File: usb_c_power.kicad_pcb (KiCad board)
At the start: 2 copper layers, 36 x 12 mm, 27 parts, among them J1 USB4085-GF-A, J2 ‎282837-2‎, Q1 IRF9358TRPBF, U1 CYPD3177

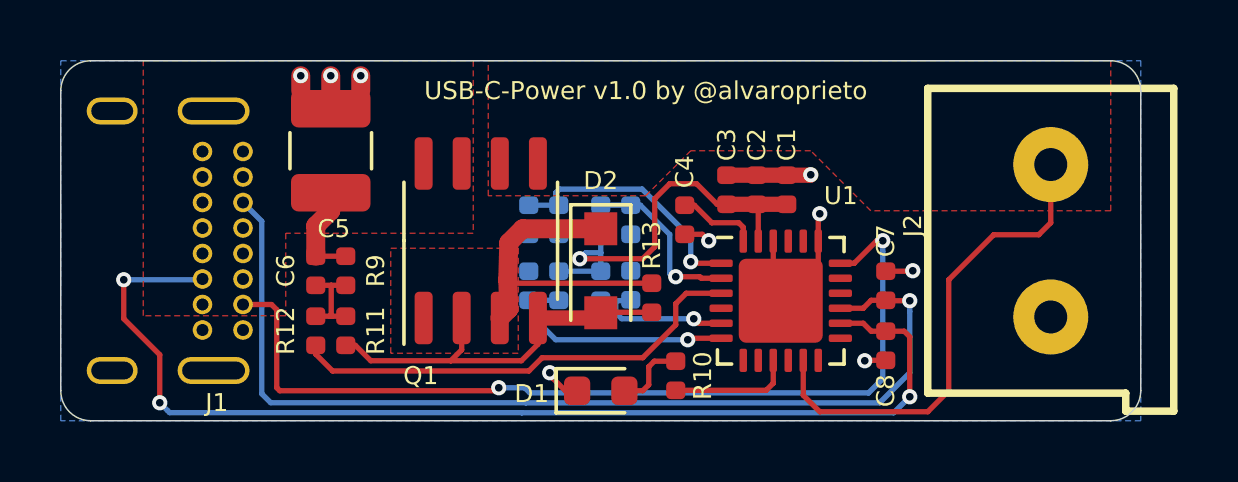
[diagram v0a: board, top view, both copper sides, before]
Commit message: Created v1.1 * much larger (0805) setting resistors * 5A rated USB-C connector * Smaller 10V zener * Paste-in-hole for usb-c
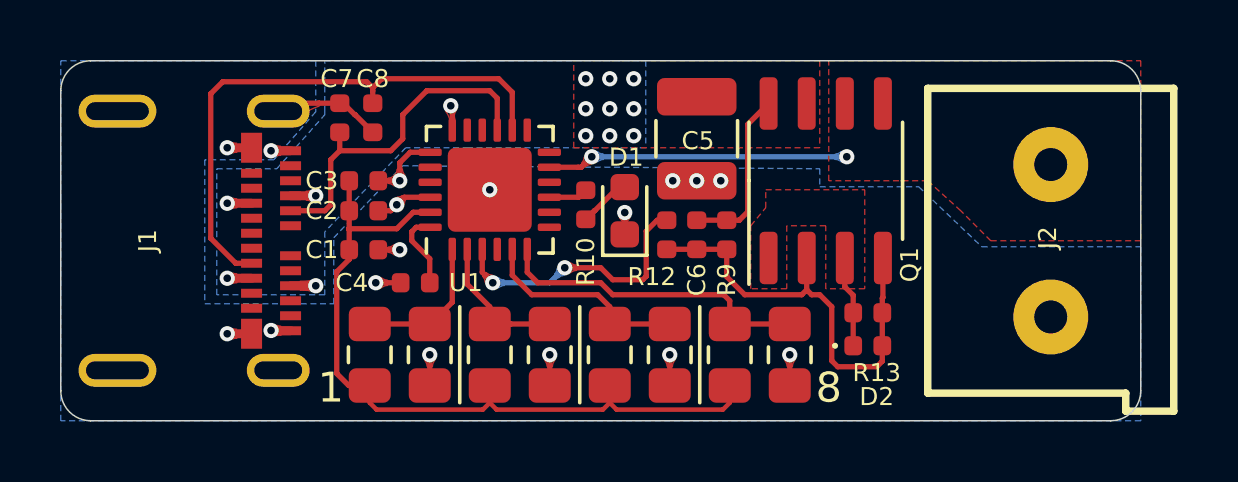
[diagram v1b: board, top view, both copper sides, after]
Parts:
- removed R11: 0, Resistor_SMD:R_0402_1005Metric
- D2: footprint Diode_SMD:D_SOD-123F -> Diode_SMD:D_0402_1005Metric
- J1: value USB4085-GF-A -> USB_C_Receptacle; footprint alvarop:USB4085-GF-A -> alvarop:MOLEX-1054500101
- R1, R2, R3, R4, R5, R6, R7, R8: footprint Resistor_SMD:R_0402_1005Metric -> Resistor_SMD:R_0805_2012Metric_Pad1.15x1.40mm_HandSolder; moved to F.Cu
- moved C7 19.0 mm to (104.3, 95.9)
- moved C8 18.7 mm to (105.4, 95.9)
- moved C1 14.2 mm to (105.1, 100.3), turned to 0 degrees
- moved C2 13.1 mm to (105.1, 99.0), turned to 0 degrees
- moved C6 12.8 mm to (116.2, 99.8)
- moved R9 12.8 mm to (117.2, 99.8)
- moved C5 12.2 mm to (116.2, 96.6), turned to 270 degrees
- moved R12 12.1 mm to (115.2, 99.8), turned to 90 degrees
- moved C3 12.1 mm to (105.1, 98.0), turned to 0 degrees
- moved Q1 11.7 mm to (120.5, 98.0)
- moved U1 10.4 mm to (109.3, 98.3), turned to 90 degrees
- moved D2 9.24 mm to (121.9, 103.5), turned to 0 degrees
- moved C4 9.23 mm to (106.8, 101.4), turned to 180 degrees
- moved R8 9.00 mm to (119.3, 103.8), turned to 270 degrees
- moved R1 7.74 mm to (105.3, 103.8)
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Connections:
- C6 pad 2: Net-(C6-Pad2) -> /FET_GATE
- R12 pad 1: Net-(C6-Pad2) -> /FET_GATE
- R9 pad 2: Net-(C6-Pad2) -> /FET_GATE
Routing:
- net /VBUS_IN: track 34.0 -> 9.85 mm, vias 2 -> 14
- net /CC1: track 33.6 -> 11.7 mm, vias 1 -> 0
- net /CC2: track 37.2 -> 18.9 mm, vias 3 -> 0
- net +3V3: track 15.4 -> 25.7 mm, vias 1 -> 0
- net /FET_SRC: track 10.7 -> 3.04 mm
- net /VBUS_FET_EN: track 15.5 -> 9.13 mm, vias 0 -> 2
- net /DC_OUT: track 16.4 -> 10.1 mm, vias 0 -> 2
- net GND: track 13.5 -> 17.6 mm, vias 9 -> 17
- net /VBUS_MIN: track 8.47 -> 4.81 mm, vias 1 -> 0
- net Net-(C6-Pad2): track 3.02 -> 0.00 mm
- net Net-(R10-Pad1): track 4.11 -> 1.31 mm
- net /ISNK_FINE: track 8.11 -> 10.7 mm, vias 1 -> 0
- net /FET_GATE: track 13.2 -> 15.2 mm
- net /ISNK_COARSE: track 5.06 -> 7.12 mm, vias 1 -> 0
- net /VBUS_MAX: track 5.79 -> 4.80 mm, vias 1 -> 0
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- added copper zone on B.Cu, net /VBUS_IN
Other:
- board text added: "1"
- board text added: "8"
- board text added: "Icoarse"
- board text added: "Ifine"
- board text removed: "Icrs"
- board text removed: "Ifin"

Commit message: Finished v1.1 and ordered from oshpark
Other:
- board text added: "USB-C-Power v1.1 by @alvaroprieto"
- board text removed: "USB-C-Power v1.0 by @alvaroprieto"
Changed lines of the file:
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@@
   (general
     (thickness 1.6)
-    (drawings 23)
+    (drawings 24)
     (tracks 199)
     (zones 0)
@@
   (title_block
     (title USB-C-Power)
-    (date 2020-03-21)
+    (date 2020-03-23)
     (rev 1.1)
     (company alvarop.com)
@@
   )
   (module Resistor_SMD:R_0402_1005Metric (layer F.Cu)
-    (at 115.2 99.8 90)
+    (at 115.2 99.85 90)
     (descr "Resistor SMD 0402 (1005 Metric), square (rectangular) end terminal, IPC_7351 nominal, (Body size source: http://www.tortai-tech.com/upload/download/2011102023233369053.pdf), generated with kicad-footprint-generator")
     (tags resistor)
@@
   )
   (module Resistor_SMD:R_0402_1005Metric (layer F.Cu)
-    (at 117.2 99.8 270)
+    (at 117.2 99.85 270)
     (descr "Resistor SMD 0402 (1005 Metric), square (rectangular) end terminal, IPC_7351 nominal, (Body size source: http://www.tortai-tech.com/upload/download/2011102023233369053.pdf), generated with kicad-footprint-generator")
     (tags resistor)
@@
   )
   (module Capacitor_SMD:C_0402_1005Metric (layer F.Cu)
-    (at 116.2 99.8 270)
+    (at 116.2 99.85 270)
     (descr "Capacitor SMD 0402 (1005 Metric), square (rectangular) end terminal, IPC_7351 nominal, (Body size source: http://www.tortai-tech.com/upload/download/2011102023233369053.pdf), generated with kicad-footprint-generator")
     (tags capacitor)
@@
     )
   )
+  (gr_poly (pts (xy 124 102.5) (xy 104 102.5) (xy 104 94.5) (xy 124 94.5)) (layer B.SilkS) (width 0.1))
   (gr_text 8 (at 120.6 104.9) (layer F.SilkS)
     (effects (font (size 1 1) (thickness 0.15)))
@@
     (effects (font (size 2 2) (thickness 0.3)) (justify mirror))
   )
-  (gr_text "USB-C-Power v1.0 by @alvaroprieto" (at 112.5 95.1) (layer B.SilkS)
+  (gr_text "USB-C-Power v1.1\nby @alvaroprieto" (at 99.7 100.2 90) (layer B.SilkS)
     (effects (font (size 0.6 0.6) (thickness 0.125)) (justify mirror))
   )
